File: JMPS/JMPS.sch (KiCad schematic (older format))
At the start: 6 parts, among them U1 74LS08, U2 74HC4078, U3 74HC238, U4 74HC238, U5 74LS08

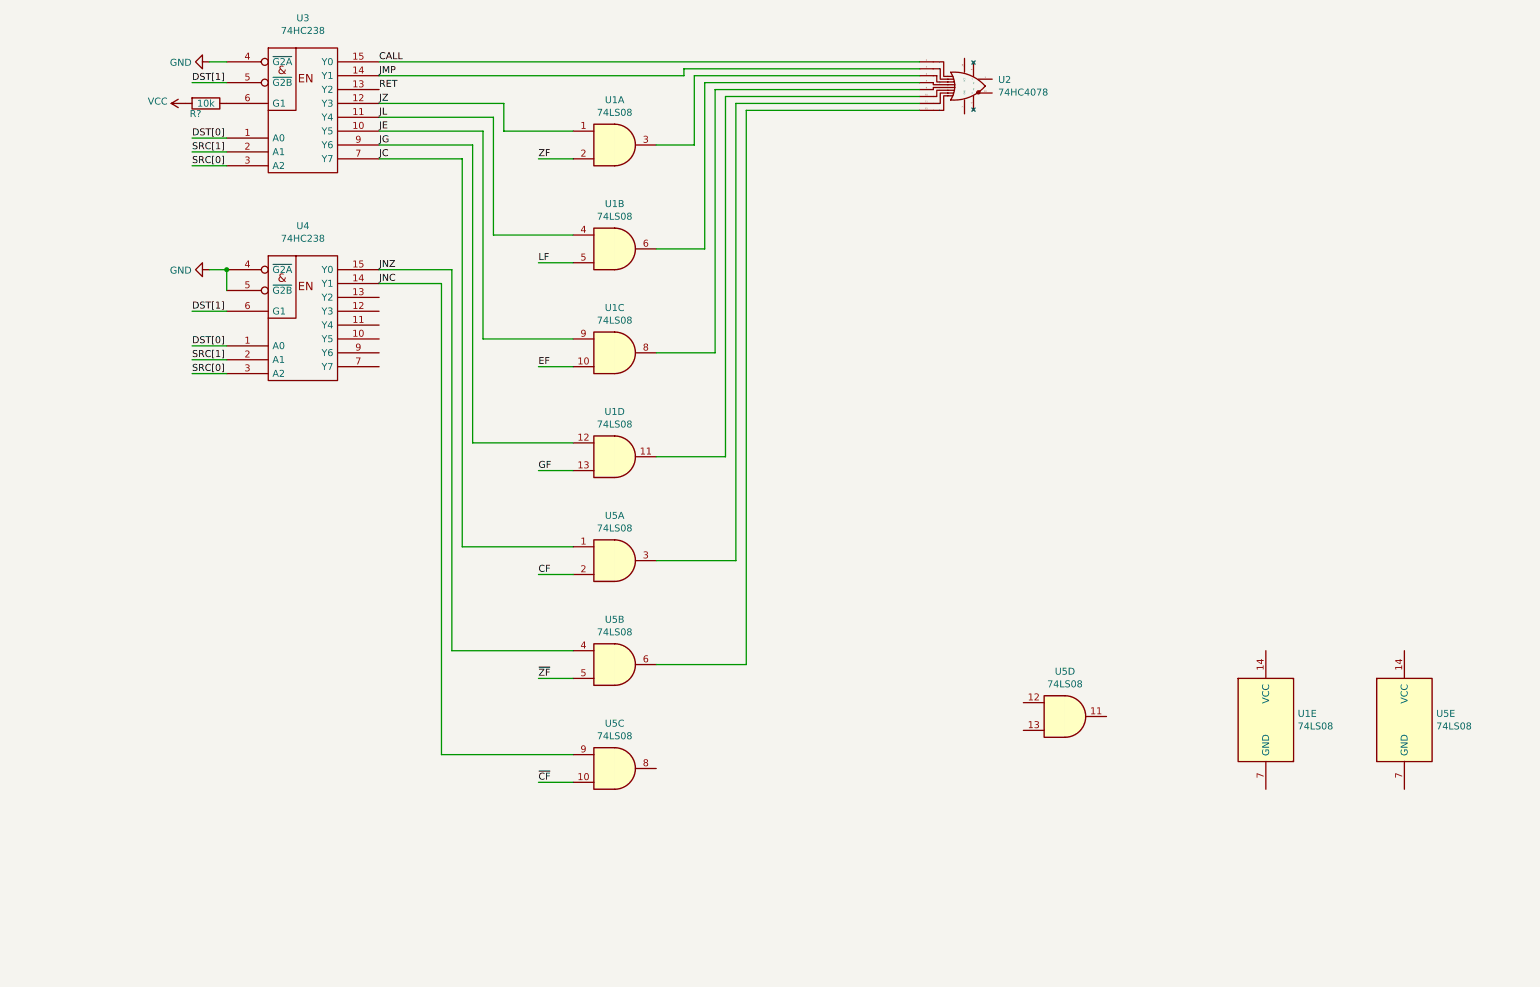
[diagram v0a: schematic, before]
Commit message: Conditional branches in work
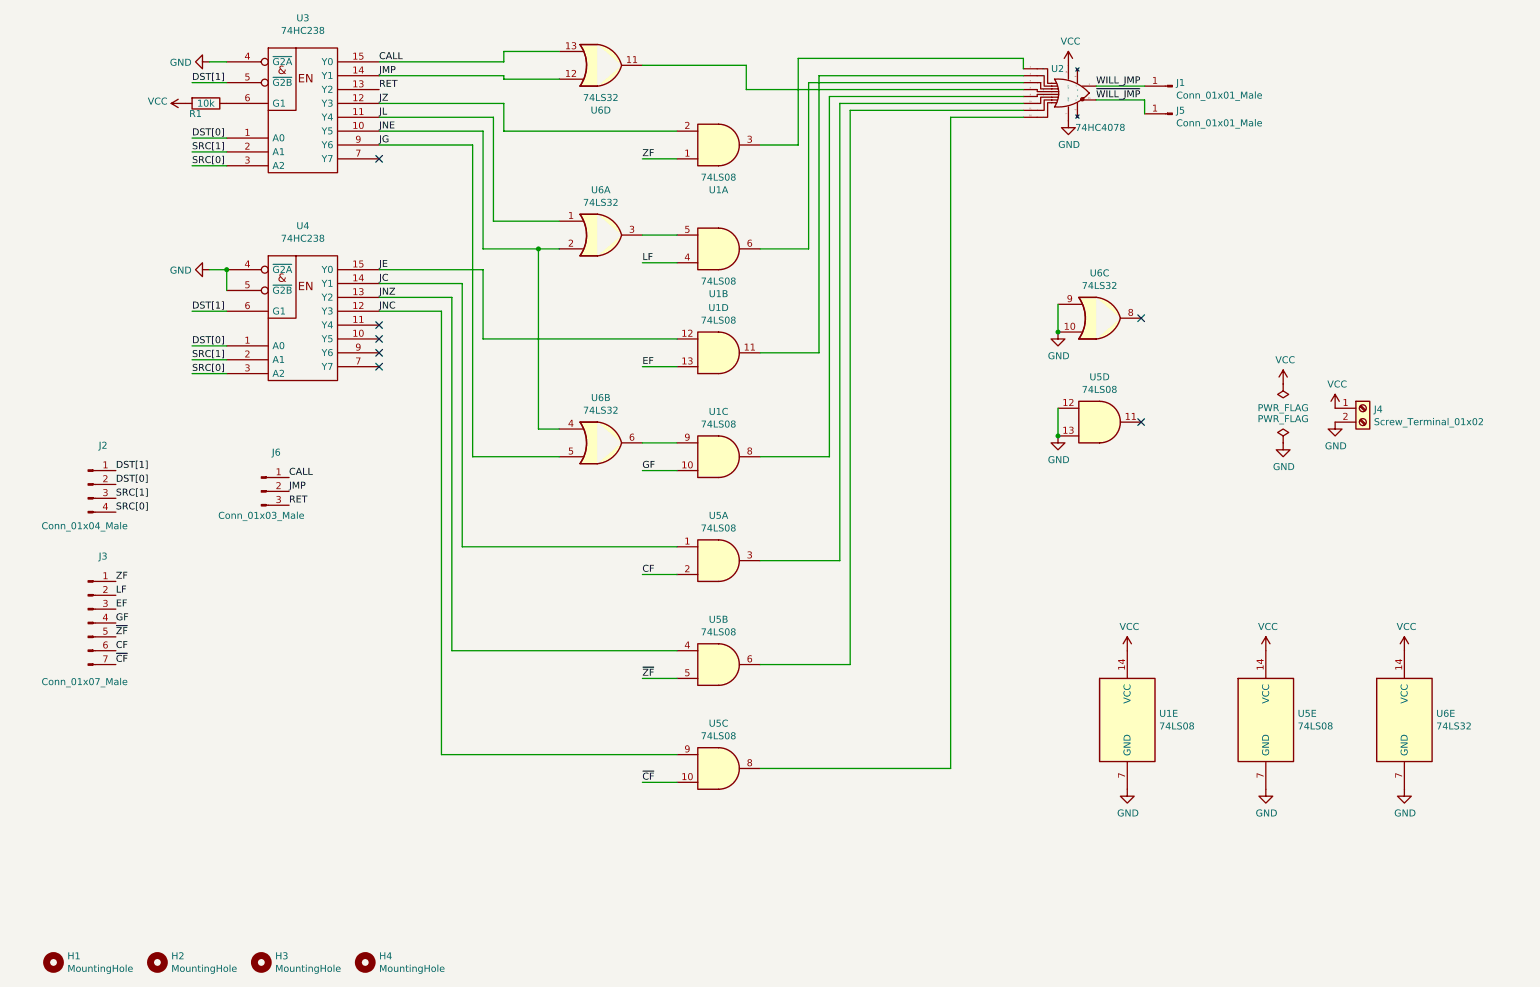
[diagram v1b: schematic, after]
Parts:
- added H1, H2, H3, H4: MountingHole, MountingHole:MountingHole_3.2mm_M3, symbol Mechanical:MountingHole
- added J1, J5: Conn_01x01_Male, Connector_PinHeader_2.54mm:PinHeader_1x01_P2.54mm_Vertical, symbol Connector:Conn_01x01_Male
- added J2: Conn_01x04_Male, Connector_PinHeader_2.54mm:PinHeader_1x04_P2.54mm_Vertical, symbol Connector:Conn_01x04_Male
- added J3: Conn_01x07_Male, Connector_PinHeader_2.54mm:PinHeader_1x07_P2.54mm_Vertical, symbol Connector:Conn_01x07_Male
- added J4: Screw_Terminal_01x02, TerminalBlock_Phoenix:TerminalBlock_Phoenix_MKDS-1,5-2_1x02_P5.00mm_Horizontal, symbol Connector:Screw_Terminal_01x02
- added J6: Conn_01x03_Male, Connector_PinHeader_2.54mm:PinHeader_1x03_P2.54mm_Vertical, symbol Connector:Conn_01x03_Male
- added U6: 74LS32, Package_DIP:DIP-14_W7.62mm_Socket, symbol 74xx:74LS32
- R1: renamed from R?; footprint (none) -> Resistor_SMD:R_0805_2012Metric_Pad1.20x1.40mm_HandSolder
- U1, U2, U5: footprint (none) -> Package_DIP:DIP-14_W7.62mm_Socket
- U3, U4: footprint (none) -> Package_DIP:DIP-16_W7.62mm_Socket
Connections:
- net CALL: now also J6.1 (Pin_1), U6.13; no longer U2.2 (A)
- net CF: now also J3.6 (Pin_6)
- net DST[0]: now also J2.2 (Pin_2)
- net DST[1]: now also J2.1 (Pin_1)
- net EF: now also U1.13, J3.3 (Pin_3); no longer U1.10
- net GF: now also U1.10, J3.4 (Pin_4); no longer U1.13
- net GND: now also U1.7 (GND), U2.7 (GND), U5.12, U5.13, U5.7 (GND), J4.2 (Pin_2), U6.10, U6.7 (GND), U6.9
- net JC: now also U4.14 (Y1); no longer U3.7 (Y7)
- net JE: now also U1.12, U4.15 (Y0); no longer U1.9, U3.10 (Y5)
- net JG: now also U6.5; no longer U1.12
- net JL: now also U6.1; no longer U1.4
- net JMP: now also J6.2 (Pin_2), U6.12; no longer U2.3 (B)
- net JNC: now also U4.12 (Y3); no longer U4.14 (Y1)
- net JNZ: now also U4.13 (Y2); no longer U4.15 (Y0)
- net JZ: now also U1.2; no longer U1.1
- net LF: now also U1.4, J3.2 (Pin_2); no longer U1.5
- net RET: now also J6.3 (Pin_3)
- net SRC[0]: now also J2.4 (Pin_4)
- net SRC[1]: now also J2.3 (Pin_3)
- net VCC: now also U1.14 (VCC), U2.14 (VCC), U5.14 (VCC), J4.1 (Pin_1), U6.14 (VCC)
- net ZF: now also U1.1, J3.1 (Pin_1); no longer U1.2
- net ~CF: now also J3.7 (Pin_7)
- net ~ZF: now also J3.5 (Pin_5)
- net at U1.3: now also U2.2 (A); no longer U2.4 (C)
- net at U1.6: now also U2.4 (C); no longer U2.5 (D)
- net at U1.11: now also U2.3 (B); no longer U2.10 (F)
- net at U5.3: now also U2.10 (F); no longer U2.11 (G)
- net at U5.6: now also U2.11 (G); no longer U2.12 (H)
- net at U5.8: now also U2.12 (H)
- net WILL_JMP: now reaches U2.1 (Y)
- net WILL_JMP: now also J1.1 (Pin_1)
- net ~WILL_JMP: now reaches U2.13 (X)
- net ~WILL_JMP: now also J5.1 (Pin_1)
- new net: U1.5, U6.3
- new net: U1.9, U6.6
- new net: U2.5 (D), U6.11
- new net JNE: U3.10 (Y5), U6.2, U6.4
- no-connect marks 0 -> 7
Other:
- moved on the sheet: U1A, U1B, U1C, U1D, U1E, U2, U5A, U5B, U5C, U5D, U5E

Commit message: Conditional branches is ready
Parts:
- added C1, C2, C3, C4: 0.1uF, Capacitor_SMD:C_0805_2012Metric_Pad1.18x1.45mm_HandSolder, symbol Device:C
- added D1: LED, LED_THT:LED_D5.0mm, symbol Device:LED
- added R2: 1k, Resistor_SMD:R_0805_2012Metric_Pad1.20x1.40mm_HandSolder, symbol Device:R
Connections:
- net CF: now also U5.1; no longer U5.2
- net EF: now also J3.4 (Pin_4); no longer J3.3 (Pin_3)
- net GF: now also J3.3 (Pin_3); no longer J3.4 (Pin_4)
- net GND: now also C1.2, C2.2, C3.2, C4.2
- net JC: now also U5.2; no longer U5.1
- net JNZ: now also U5.5; no longer U5.4
- net VCC: now also C1.1, C2.1, C3.1, C4.1, R2.2
- net ~WILL_JMP: now also D1.1 (K)
- net ~ZF: now also U5.4; no longer U5.5
- new net: D1.2 (A), R2.1
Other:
- moved on the sheet: J4, U5D

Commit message: SWAP CF & ZF
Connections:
- net ~CF: now also J3.5 (Pin_5); no longer J3.7 (Pin_7)
- net ~ZF: now also J3.7 (Pin_7); no longer J3.5 (Pin_5)
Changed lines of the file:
@@
 Text Label 1200 5250 0    50   ~ 0
 CF
+Text Label 1200 5350 0    50   ~ 0
+~ZF
 Text Label 1200 5150 0    50   ~ 0
-~ZF
-Text Label 1200 5350 0    50   ~ 0
 ~CF
 NoConn ~ 3100 2900

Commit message: Fix pins & text
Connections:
- net CF: now also J3.5 (Pin_5); no longer J3.6 (Pin_6)
- net EF: now also J3.3 (Pin_3); no longer J3.4 (Pin_4)
- net GF: now also J3.2 (Pin_2); no longer J3.3 (Pin_3)
- net LF: now also J3.1 (Pin_1); no longer J3.2 (Pin_2)
- net ZF: now also J3.7 (Pin_7); no longer J3.1 (Pin_1)
- net ~CF: now also J3.4 (Pin_4); no longer J3.5 (Pin_5)
- net ~ZF: now also J3.6 (Pin_6); no longer J3.7 (Pin_7)
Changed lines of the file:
@@
 	1    0    0    -1
 $EndComp
+Text Label 1200 5350 0    50   ~ 0
+ZF
 Text Label 1200 4750 0    50   ~ 0
-ZF
+LF
+Text Label 1200 4950 0    50   ~ 0
+EF
 Text Label 1200 4850 0    50   ~ 0
-LF
+GF
+Text Label 1200 5150 0    50   ~ 0
+CF
+Text Label 1200 5250 0    50   ~ 0
+~ZF
 Text Label 1200 5050 0    50   ~ 0
-EF
-Text Label 1200 4950 0    50   ~ 0
-GF
-Text Label 1200 5250 0    50   ~ 0
-CF
-Text Label 1200 5350 0    50   ~ 0
-~ZF
-Text Label 1200 5150 0    50   ~ 0
 ~CF
 NoConn ~ 3100 2900

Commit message: JUMPS. Lost signal.
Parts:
- added J7: Conn_01x01_Male, Connector_PinHeader_2.54mm:PinHeader_1x01_P2.54mm_Vertical, symbol Connector:Conn_01x01_Male
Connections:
- net DST[1]: now also U3.4 (~G2A); no longer U3.5 (~G2B)
- net GND: no longer U3.4 (~G2A), U4.4 (~G2A)
- new net ~BRANCH: J7.1 (Pin_1), U3.5 (~G2B), U4.4 (~G2A)
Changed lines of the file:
@@
-$EndComp
-$Comp
-L power:GND #PWR01
-U 1 1 63F1268E
-P 1875 1000
-F 0 "#PWR01" H 1875 750 50  0001 C CNN
-F 1 "GND" V 1880 872 50  0000 R CNN
-F 2 "" H 1875 1000 50  0001 C CNN
-F 3 "" H 1875 1000 50  0001 C CNN
-	1    1875 1000
-	0    1    1    0
 $EndComp
 $Comp
@@
 Text Label 1750 1550 0    50   ~ 0
 DST[0]
-Text Label 1750 1150 0    50   ~ 0
+Text Label 1750 1000 0    50   ~ 0
 DST[1]
 Text Label 1750 1750 0    50   ~ 0
 SRC[0]
 Wire Wire Line
-	1750 1150 2000 1150
+	1750 1000 2000 1000
 Text Label 1750 1650 0    50   ~ 0
 SRC[1]
@@
 L power:GND #PWR0101
 U 1 1 63F7064B
-P 1875 2500
-F 0 "#PWR0101" H 1875 2250 50  0001 C CNN
-F 1 "GND" V 1880 2372 50  0000 R CNN
-F 2 "" H 1875 2500 50  0001 C CNN
-F 3 "" H 1875 2500 50  0001 C CNN
-	1    1875 2500
+P 2000 2650
+F 0 "#PWR0101" H 2000 2400 50  0001 C CNN
+F 1 "GND" V 2005 2522 50  0000 R CNN
+F 2 "" H 2000 2650 50  0001 C CNN
+F 3 "" H 2000 2650 50  0001 C CNN
+	1    2000 2650
 	0    1    1    0
 $EndComp
-Wire Wire Line
-	1875 2500 2000 2500
-Wire Wire Line
-	2000 2500 2000 2650
-Connection ~ 2000 2500
-Wire Wire Line
-	1875 1000 2000 1000
 $Comp
 L Device:R R1
@@
 	1    0    0    -1
 $EndComp
+Text Label 1650 1150 0    50   ~ 0
+~BRANCH
+Wire Wire Line
+	1650 1150 2000 1150
+Text Label 1650 2500 0    50   ~ 0
+~BRANCH
+Wire Wire Line
+	1650 2500 2000 2500
+$Comp
+L Connector:Conn_01x01_Male J7
+U 1 1 640FA758
+P 675 1000
+F 0 "J7" H 783 1181 50  0000 C CNN
+F 1 "Conn_01x01_Male" H 825 875 50  0000 C CNN
+F 2 "Connector_PinHeader_2.54mm:PinHeader_1x01_P2.54mm_Vertical" H 675 1000 50  0001 C CNN
+F 3 "~" H 675 1000 50  0001 C CNN
+	1    675  1000
+	1    0    0    -1
+$EndComp
+Text Label 875  1000 0    50   ~ 0
+~BRANCH
 $EndSCHEMATC
